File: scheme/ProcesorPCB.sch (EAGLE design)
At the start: 25 parts, among them X1 22-23-2101, X10 22-23-2021, X11 22-23-2021, X12 22-23-2051, X2 22-23-2101, X3 22-23-2101, X4 22-23-2101, X5 22-23-2051, X7 22-23-2021, X8 22-23-2031, X9 22-23-2021

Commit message: Work on PCB
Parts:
- removed X1, X2, X3, X4: 22-23-2101, con-molex:22-23-2101
- removed X10, X11, X7, X9: 22-23-2021, con-molex:22-23-2021
- removed X5: 22-23-2051, con-molex:22-23-2051
- removed X6: (no value), con-ptr500:AK500/2
- removed X8: 22-23-2031, con-molex:22-23-2031
- added JP10, JP11, JP12, JP13, JP14, JP15, JP16, JP17, JP18, JP7, JP8, JP9: (no value), jumper:JP2E
- JP1: device jumper:JP4E -> jumper:JP10Q
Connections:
- removed net DI: JP1.3, X5-1.S
- removed net DO: X5-4.S
- removed net E2: U$1.RC5/CCP1/P1A, X1-9.S
- removed net E3: X2-4.S
- removed net E4: X2-9.S
- removed net E5: X3-4.S
- removed net E6: X3-9.S
- removed net E8: JP1.1, X4-9.S
- removed net EV11: X2-6.S
- removed net EV12: X2-8.S
- removed net EV17: X3-6.S
- removed net EV18: X3-8.S
- removed net N$29: X3-10.S
- removed net Y3: X2-5.S
- removed net Y4: X2-7.S
- removed net Y5: X3-5.S
- removed net Y6: X3-7.S
- new net CCP: JP1.6, U$1.RC5/CCP1/P1A
- new net N$7: R1.1
- new net N$9: JP3.3, JP3.4, JP6.1
- net +5V: now also JP1.4; no longer R1.1, R2.1, X10-1.S, X11-1.S, X4-1.S, X6-1.KL, X7-1.S, X9-1.S
- net CKL: no longer X5-2.S
- net E1: no longer X1-4.S
- net E7: no longer X4-6.S
- net EV5: no longer X1-6.S
- net EV6: no longer X1-8.S
- net GND: now also JP1.10; no longer JP3.3, JP3.4, JP6.1, X10-2.S, X11-2.S, X4-2.S, X5-5.S, X6-2.KL, X7-2.S, X8-1.S, X9-2.S
- net LD: no longer X5-3.S
- net PGC,S1: no longer X1-2.S, X2-2.S, X3-2.S, X4-4.S
- net PGD,S2: no longer X1-1.S, X2-1.S, X3-1.S, X4-3.S
- net RX: no longer X8-2.S
- net S0: no longer X1-3.S, X2-3.S, X3-3.S, X4-5.S
- net SDA: no longer JP1.4
- net SDO: no longer JP1.2
- net TX: no longer X8-3.S
- net VPP,Y7: no longer X4-7.S
- net Y1: no longer X1-5.S
- net Y2: no longer X1-7.S
- net Y8: no longer X4-8.S

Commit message: Hmm not Saved
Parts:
- added U1: UA78L05ACPKG3, TI-Eagle_library:UA78L05ACPKG3
- added X1: 22-23-2031, con-molex:22-23-2031
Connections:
- removed net CKL: U$1.RB6/SCK/SCL
- removed net E1: U$1.RC0/AN4/C2IN+
- removed net E7: U$1.RA4/AN3/T1G/OSC2/CLKOUT
- removed net EV5: U$1.RC2/AN6/C12IN2-/P1D
- removed net LD: U$1.RC6/AN8/SS
- removed net N$7: R1.1
- removed net PGC,S1: U$1.RA1/AN1/C12IN0-/VREF/ICSPCLK, X12-4.S
- removed net PGD,S2: U$1.RA0/AN0/C1IN+/ICSPDAT/ULPWU, X12-3.S
- removed net S0: U$1.RA2/AN2/T0CKI/INT/C1OUT
- removed net SDA: U$1.RB4/AN10/SDI/SDA
- removed net SDO: U$1.RC7/AN9/SDO
- removed net Y1: U$1.RC1/AN5/C12IN1-
- removed net Y2: U$1.RC3/AN7C12IN3-/P1C
- new net +24V: U1.INPUT, X1-3.S
- new net AN0,PGD: JP7.2, U$1.RA0/AN0/C1IN+/ICSPDAT/ULPWU, X12-3.S
- new net AN1,PGC: JP8.2, U$1.RA1/AN1/C12IN0-/VREF/ICSPCLK, X12-4.S
- new net AN10: JP17.2, U$1.RB4/AN10/SDI/SDA
- new net AN11: JP18.2, U$1.RB5/AN11/RX/DT
- new net AN2: JP9.2, U$1.RA2/AN2/T0CKI/INT/C1OUT
- new net AN3: JP10.2, U$1.RA4/AN3/T1G/OSC2/CLKOUT
- new net AN4: JP11.2, U$1.RC0/AN4/C2IN+
- new net AN5: JP12.2, U$1.RC1/AN5/C12IN1-
- new net AN6: JP13.2, U$1.RC2/AN6/C12IN2-/P1D
- new net AN7: JP14.2, U$1.RC3/AN7C12IN3-/P1C
- new net AN8: JP15.2, U$1.RC6/AN8/SS
- new net AN9: JP16.2, U$1.RC7/AN9/SDO
- new net OUT: U$1.RB6/SCK/SCL, X1-2.S
- net +5V: now also JP10.1, JP11.1, JP12.1, JP13.1, JP14.1, JP15.1, JP16.1, JP17.1, JP18.1, JP7.1, JP8.1, JP9.1, U1.OUTPUT; no longer JP4.1, LED3.A
- net GND: now also JP10.3, JP11.3, JP12.3, JP13.3, JP14.3, JP15.3, JP16.3, JP17.3, JP18.3, JP7.3, JP8.3, JP9.3, U1.COM, U1.COM_1, X1-1.S; no longer R3.1
- net RX: no longer U$1.RB5/AN11/RX/DT
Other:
- moved on the sheet: JP1, LED3, R3

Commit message: PCB borad almost finished.
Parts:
- removed JP3, JP5, JP6: (no value), jumper:JP4E
- removed JP4: (no value), jumper:JP1E
- removed LED1: Cervena, led:LED5MM
- removed LED2, LED3: Zenena, led:LED5MM
- removed R2, R3: (no value), rcl:R-EU_R0805W
- added C1: 1uF, resistor:C-EU025-030X050
- added C2: 0.33uF, resistor:C-EU025-030X050
- added RN1, RN2: 15K, resistor-net:RN06
- added RN3: 22k, resistor-net:RN06
- added RN4: 22K, resistor-net:RN06
- R1: device rcl:R-EU_R0805W -> resistor:R-EU_0207/10
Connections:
- removed net AN11: JP18.2, U$1.RB5/AN11/RX/DT
- removed net N$3: JP6.4, LED2.C
- removed net N$4: JP6.3, LED1.C
- removed net N$5: LED2.A, R2.2
- removed net N$6: LED1.A, R1.2
- removed net N$8: LED3.C, R3.2
- removed net N$9: JP3.3, JP3.4, JP6.1
- removed net RX: JP2.4, JP5.4
- new net AN11,RX: JP18.2, JP2.4, RN1.7, RN3.7, U$1.RB5/AN11/RX/DT
- net +24V: now also R1.2; no longer U1.INPUT
- net +5V: now also C1.1, RN3.1, RN4.1
- net AN0,PGD: now also RN2.7, RN4.7
- net AN1,PGC: now also RN2.6, RN4.6
- net AN10: now also RN1.3, RN3.3
- net AN2: now also RN2.5, RN4.5
- net AN3: now also RN1.2, RN3.2
- net AN4: now also RN2.4, RN4.4
- net AN5: now also RN2.3, RN4.3
- net AN6: now also RN2.2, RN4.2
- net AN7: now also RN1.4, RN3.4
- net AN8: now also RN1.5, RN3.5
- net AN9: now also RN1.6, RN3.6
- net GND: now also C1.2, C2.2, JP2.2, RN1.1, RN2.1
- net N$2: now also C2.1, R1.1, U1.INPUT; no longer JP3.1, JP3.2, JP4.2, JP6.2
- net TX: no longer JP5.3
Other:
- moved on the sheet: JP10, JP11, JP12, JP13, JP14, JP15, JP16, JP17, JP18, JP2, JP7, JP8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

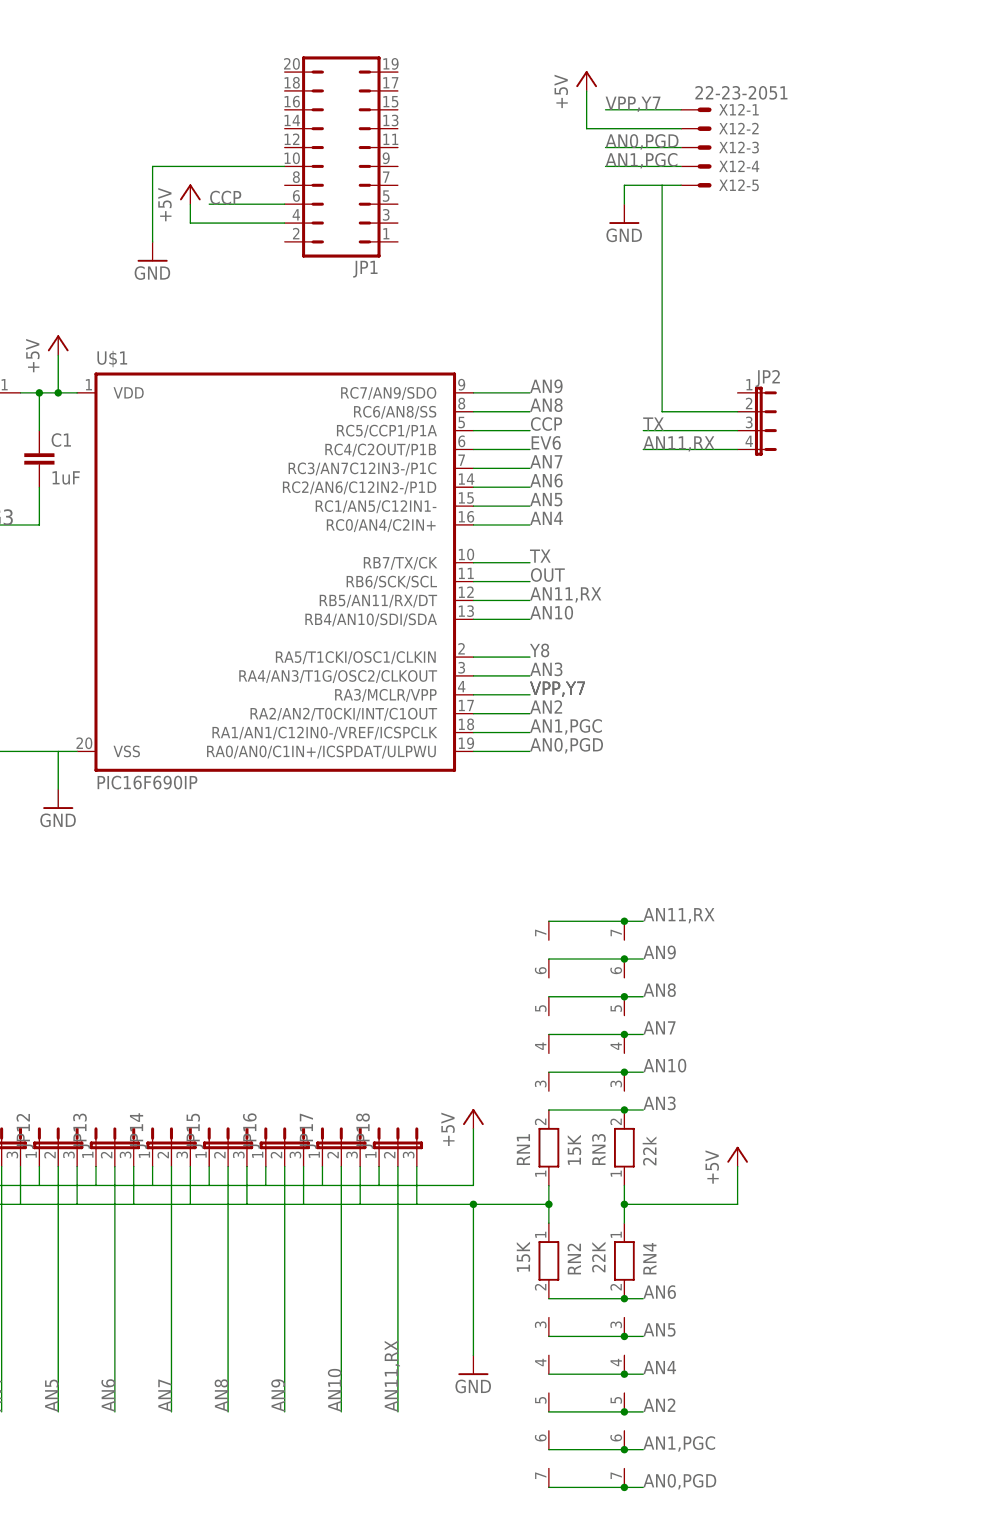
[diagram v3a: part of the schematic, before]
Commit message: Add documentation for LM358, update schema, add adc settings from previous project to file orig_mail.c
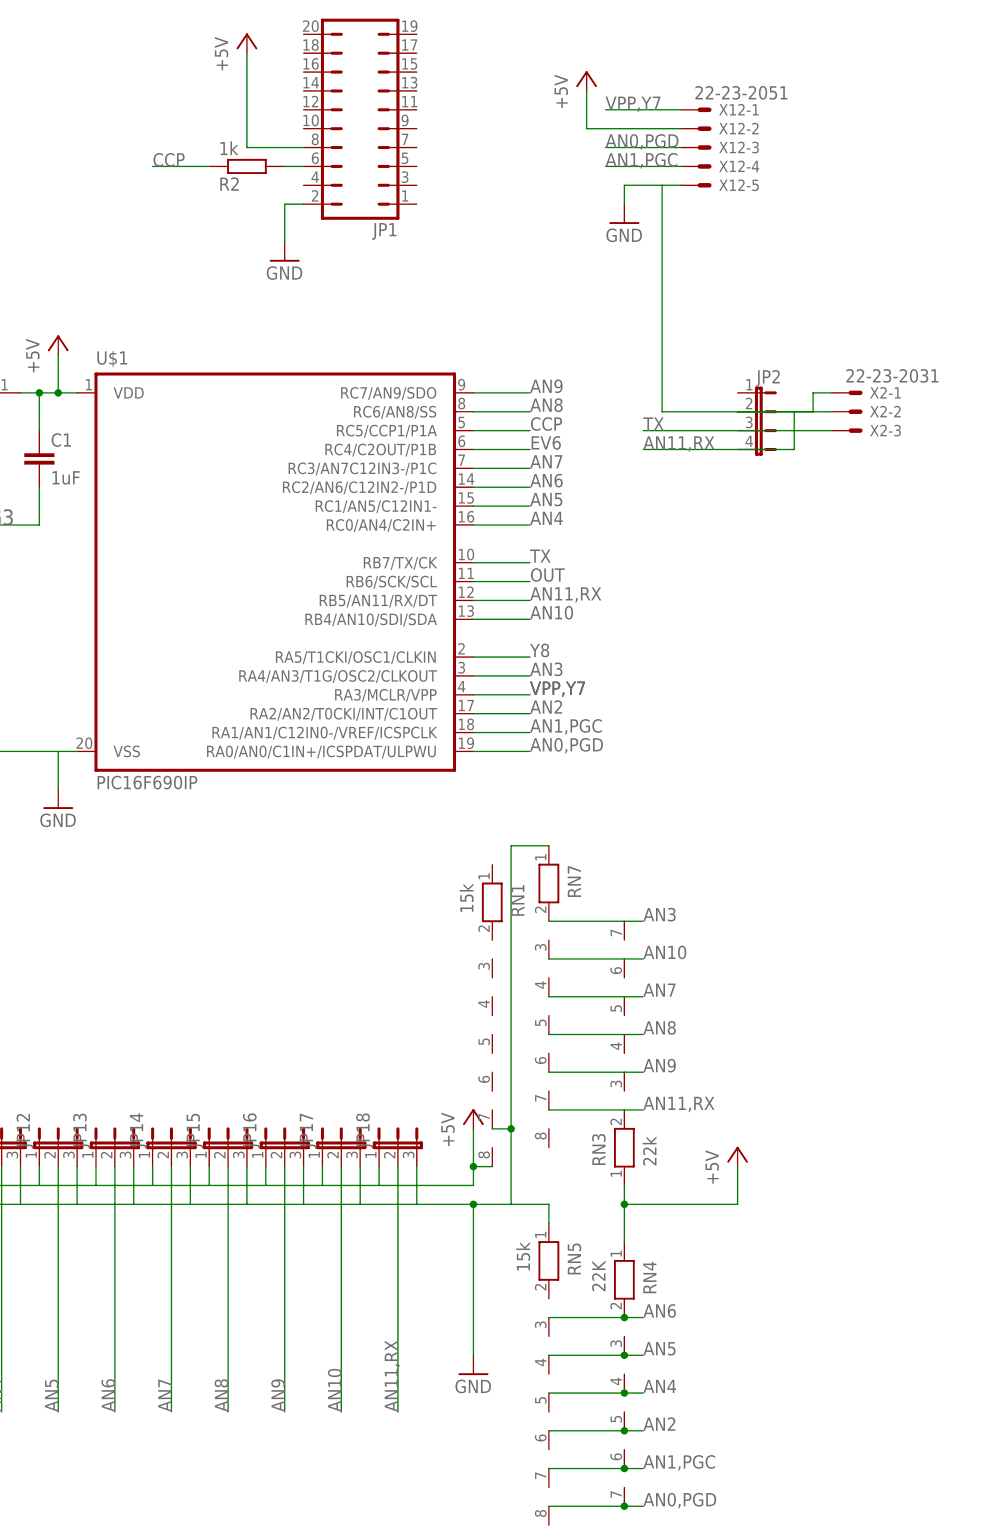
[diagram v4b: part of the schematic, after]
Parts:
- removed RN2: 15K, resistor-net:RN06
- added R2: 1k, resistor:R-EU_0204/7
- added RN5: 15k, resistor-net:RN07
- added RN7: (no value), resistor-net:RN07
- added X2: 22-23-2031, con-molex:22-23-2031
- RN1: value 15K -> 15k; device resistor-net:RN06 -> resistor-net:RN07
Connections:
- new net N$4: JP1.6, R2.2
- net +5V: now also JP1.8, RN1.8; no longer JP1.4
- net AN0,PGD: no longer RN2.7
- net AN1,PGC: no longer RN2.6
- net AN10: now also RN3.6, RN7.3; no longer RN1.3, RN3.3
- net AN11,RX: now also RN3.2, RN7.7, X2-2.S; no longer RN1.7, RN3.7
- net AN2: no longer RN2.5
- net AN3: now also RN3.7, RN7.2; no longer RN1.2, RN3.2
- net AN4: no longer RN2.4
- net AN5: no longer RN2.3
- net AN6: no longer RN2.2
- net AN7: now also RN3.5, RN7.4; no longer RN1.4, RN3.4
- net AN8: now also RN3.4, RN7.5; no longer RN1.5, RN3.5
- net AN9: now also RN3.3, RN7.6; no longer RN1.6, RN3.6
- net CCP: now also R2.1; no longer JP1.6
- net GND: now also JP1.2, RN1.7, RN5.1, RN7.1, X2-1.S; no longer JP1.10, RN1.1, RN2.1
- net TX: now also X2-3.S
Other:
- moved on the sheet: JP1, RN4
